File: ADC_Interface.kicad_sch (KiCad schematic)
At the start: 42 parts, among them U401 ADAU1978, U402 TLV333, X401 12.288MHz

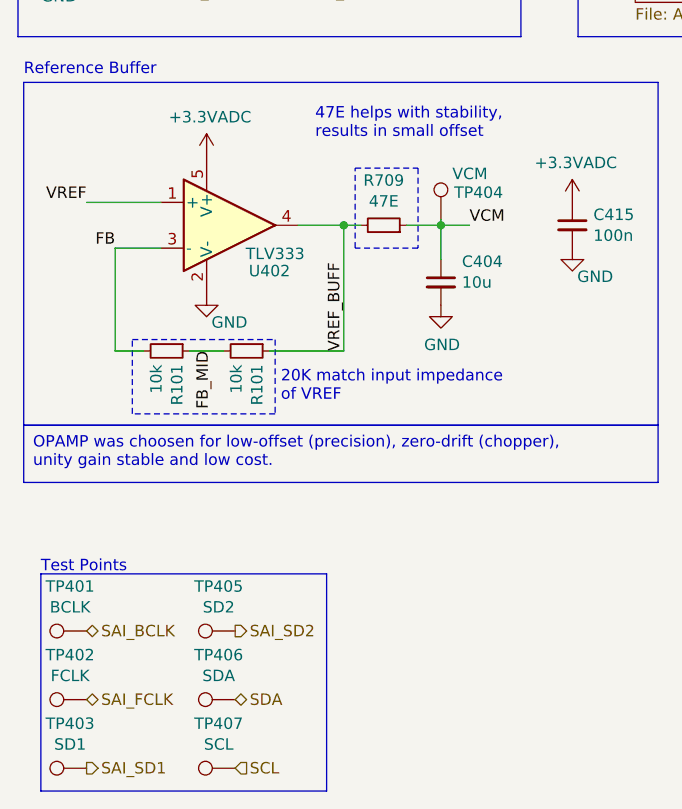
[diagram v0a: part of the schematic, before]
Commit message: (pcb) route power
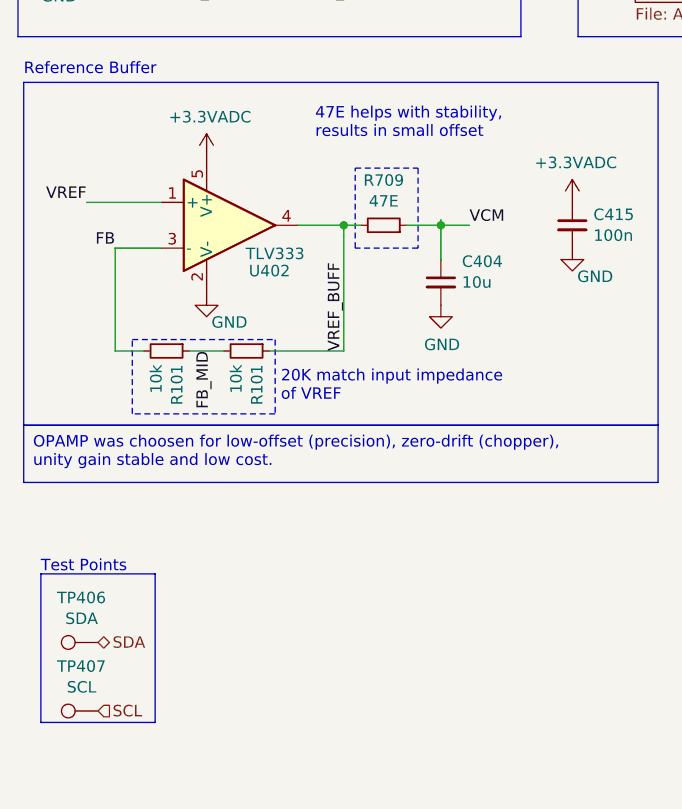
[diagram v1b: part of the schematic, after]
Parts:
- removed TP401: BCLK, TestPoint:TestPoint_Pad_D1.0mm, symbol Connector:TestPoint
- removed TP402: FCLK, TestPoint:TestPoint_Pad_D1.0mm, symbol Connector:TestPoint
- removed TP403: SD1, TestPoint:TestPoint_Pad_D1.0mm, symbol Connector:TestPoint
- removed TP404: VCM, TestPoint:TestPoint_Pad_D1.0mm, symbol Connector:TestPoint
- removed TP405: SD2, TestPoint:TestPoint_Pad_D1.0mm, symbol Connector:TestPoint
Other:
- moved on the sheet: TP406, TP407
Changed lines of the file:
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@@
     (fill (type none))
   )
-  (rectangle (start 20.32 152.4) (end 52.07 176.53)
+  (rectangle (start 20.32 152.4) (end 33.02 168.91)
     (stroke (width 0) (type default))
     (fill (type none))
@@
     (effects (font (size 1.27 1.27)) (justify left))
   )
-  (hierarchical_label "SDA" (shape bidirectional) (at 41.91 166.37 0) (fields_autoplaced)
-    (effects (font (size 1.27 1.27)) (justify left))
-  )
-  (hierarchical_label "SAI_BCLK" (shape bidirectional) (at 25.4 158.75 0) (fields_autoplaced)
-    (effects (font (size 1.27 1.27)) (justify left))
-  )
-  (hierarchical_label "SAI_SD2" (shape output) (at 41.91 158.75 0) (fields_autoplaced)
-    (effects (font (size 1.27 1.27)) (justify left))
-  )
-  (hierarchical_label "SAI_SD1" (shape output) (at 25.4 173.99 0) (fields_autoplaced)
+  (hierarchical_label "SDA" (shape bidirectional) (at 26.67 160.02 0) (fields_autoplaced)
     (effects (font (size 1.27 1.27)) (justify left))
   )
@@
     (effects (font (size 1.27 1.27)) (justify left))
   )
-  (hierarchical_label "SCL" (shape input) (at 41.91 173.99 0) (fields_autoplaced)
+  (hierarchical_label "SCL" (shape input) (at 26.67 167.64 0) (fields_autoplaced)
     (effects (font (size 1.27 1.27)) (justify left))
   )
   (hierarchical_label "SCL" (shape input) (at 260.35 104.14 0) (fields_autoplaced)
-    (effects (font (size 1.27 1.27)) (justify left))
-  )
-  (hierarchical_label "SAI_FCLK" (shape bidirectional) (at 25.4 166.37 0) (fields_autoplaced)
     (effects (font (size 1.27 1.27)) (justify left))
   )
@@
     )
   )
-  (symbol (lib_id "Connector:TestPoint") (at 64.77 113.03 0) (unit 1)
-    (in_bom yes) (on_board yes) (dnp no)
-    (property "Reference" "TP404" (at 66.2432 110.0328 0)
-      (effects (font (size 1.27 1.27)) (justify left))
-    )
-    (property "Value" "VCM" (at 66.04 107.95 0)
-      (effects (font (size 1.27 1.27)) (justify left))
-    )
-    (property "Footprint" "TestPoint:TestPoint_Pad_D1.0mm" (at 69.85 113.03 0)
-      (effects (font (size 1.27 1.27)) hide)
-    )
-    (property "Datasheet" "~" (at 69.85 113.03 0)
-      (effects (font (size 1.27 1.27)) hide)
-    )
-    (pin "1")
-    (instances
-      (project "kleinvoet"
-        (path "/4185c36c-c66e-4dbd-be5d-841e551f4885/00000000-0000-0000-0000-00005ee5ecad"
-          (reference "TP404") (unit 1)
-        )
-      )
-    )
-  )
-  (symbol (lib_id "Connector:TestPoint") (at 25.4 158.75 90) (unit 1)
-    (in_bom yes) (on_board yes) (dnp no)
-    (property "Reference" "TP401" (at 23.5712 153.797 90)
-      (effects (font (size 1.27 1.27)))
-    )
-    (property "Value" "BCLK" (at 23.5712 156.1084 90)
-      (effects (font (size 1.27 1.27)))
-    )
-    (property "Footprint" "TestPoint:TestPoint_Pad_D1.0mm" (at 25.4 153.67 0)
-      (effects (font (size 1.27 1.27)) hide)
-    )
-    (property "Datasheet" "~" (at 25.4 153.67 0)
-      (effects (font (size 1.27 1.27)) hide)
-    )
-    (pin "1")
-    (instances
-      (project "kleinvoet"
-        (path "/4185c36c-c66e-4dbd-be5d-841e551f4885/00000000-0000-0000-0000-00005ee5ecad"
-          (reference "TP401") (unit 1)
-        )
-      )
-    )
-  )
-  (symbol (lib_id "Connector:TestPoint") (at 25.4 166.37 90) (unit 1)
-    (in_bom yes) (on_board yes) (dnp no)
-    (property "Reference" "TP402" (at 23.5712 161.417 90)
-      (effects (font (size 1.27 1.27)))
-    )
-    (property "Value" "FCLK" (at 23.5712 163.7284 90)
-      (effects (font (size 1.27 1.27)))
-    )
-    (property "Footprint" "TestPoint:TestPoint_Pad_D1.0mm" (at 25.4 161.29 0)
-      (effects (font (size 1.27 1.27)) hide)
-    )
-    (property "Datasheet" "~" (at 25.4 161.29 0)
-      (effects (font (size 1.27 1.27)) hide)
-    )
-    (pin "1")
-    (instances
-      (project "kleinvoet"
-        (path "/4185c36c-c66e-4dbd-be5d-841e551f4885/00000000-0000-0000-0000-00005ee5ecad"
-          (reference "TP402") (unit 1)
-        )
-      )
-    )
-  )
-  (symbol (lib_id "Connector:TestPoint") (at 25.4 173.99 90) (unit 1)
-    (in_bom yes) (on_board yes) (dnp no)
-    (property "Reference" "TP403" (at 23.5712 169.037 90)
-      (effects (font (size 1.27 1.27)))
-    )
-    (property "Value" "SD1" (at 23.5712 171.3484 90)
-      (effects (font (size 1.27 1.27)))
-    )
-    (property "Footprint" "TestPoint:TestPoint_Pad_D1.0mm" (at 25.4 168.91 0)
-      (effects (font (size 1.27 1.27)) hide)
-    )
-    (property "Datasheet" "~" (at 25.4 168.91 0)
-      (effects (font (size 1.27 1.27)) hide)
-    )
-    (pin "1")
-    (instances
-      (project "kleinvoet"
-        (path "/4185c36c-c66e-4dbd-be5d-841e551f4885/00000000-0000-0000-0000-00005ee5ecad"
-          (reference "TP403") (unit 1)
-        )
-      )
-    )
-  )
-  (symbol (lib_id "Connector:TestPoint") (at 41.91 158.75 90) (unit 1)
-    (in_bom yes) (on_board yes) (dnp no)
-    (property "Reference" "TP405" (at 40.0812 153.797 90)
-      (effects (font (size 1.27 1.27)))
-    )
-    (property "Value" "SD2" (at 40.0812 156.1084 90)
-      (effects (font (size 1.27 1.27)))
-    )
-    (property "Footprint" "TestPoint:TestPoint_Pad_D1.0mm" (at 41.91 153.67 0)
-      (effects (font (size 1.27 1.27)) hide)
-    )
-    (property "Datasheet" "~" (at 41.91 153.67 0)
-      (effects (font (size 1.27 1.27)) hide)
-    )
-    (pin "1")
-    (instances
-      (project "kleinvoet"
-        (path "/4185c36c-c66e-4dbd-be5d-841e551f4885/00000000-0000-0000-0000-00005ee5ecad"
-          (reference "TP405") (unit 1)
-        )
-      )
-    )
-  )
-  (symbol (lib_id "Connector:TestPoint") (at 41.91 166.37 90) (unit 1)
-    (in_bom yes) (on_board yes) (dnp no)
-    (property "Reference" "TP406" (at 40.0812 161.417 90)
-      (effects (font (size 1.27 1.27)))
-    )
-    (property "Value" "SDA" (at 40.0812 163.7284 90)
-      (effects (font (size 1.27 1.27)))
-    )
-    (property "Footprint" "TestPoint:TestPoint_Pad_D1.0mm" (at 41.91 161.29 0)
-      (effects (font (size 1.27 1.27)) hide)
-    )
-    (property "Datasheet" "~" (at 41.91 161.29 0)
+  (symbol (lib_id "Connector:TestPoint") (at 26.67 160.02 90) (unit 1)
+    (in_bom yes) (on_board yes) (dnp no)
+    (property "Reference" "TP406" (at 24.8412 155.067 90)
+      (effects (font (size 1.27 1.27)))
+    )
+    (property "Value" "SDA" (at 24.8412 157.3784 90)
+      (effects (font (size 1.27 1.27)))
+    )
+    (property "Footprint" "TestPoint:TestPoint_Pad_D1.0mm" (at 26.67 154.94 0)
+      (effects (font (size 1.27 1.27)) hide)
+    )
+    (property "Datasheet" "~" (at 26.67 154.94 0)
       (effects (font (size 1.27 1.27)) hide)
     )
@@
     )
   )
-  (symbol (lib_id "Connector:TestPoint") (at 41.91 173.99 90) (unit 1)
-    (in_bom yes) (on_board yes) (dnp no)
-    (property "Reference" "TP407" (at 40.0812 169.037 90)
-      (effects (font (size 1.27 1.27)))
-    )
-    (property "Value" "SCL" (at 40.0812 171.3484 90)
-      (effects (font (size 1.27 1.27)))
-    )
-    (property "Footprint" "TestPoint:TestPoint_Pad_D1.0mm" (at 41.91 168.91 0)
-      (effects (font (size 1.27 1.27)) hide)
-    )
-    (property "Datasheet" "~" (at 41.91 168.91 0)
-      (effects (font (size 1.27 1.27)) hide)
-    )
+  (symbol (lib_id "Connector:TestPoint") (at 26.67 167.64 90) (unit 1)
+    (in_bom yes) (on_board yes) (dnp no)
+    (property "Reference" "TP407" (at 24.8412 162.687 90)
+      (effects (font (size 1.27 1.27)))
+    )
+    (property "Value" "SCL" (at 24.8412 164.9984 90)
+      (effects (font (size 1.27 1.27)))
+    )
+    (property "Footprint" "TestPoint:TestPoint_Pad_D1.0mm" (at 26.67 162.56 0)
+      (effects (font (size 1.27 1.27)) hide)
+    )
+    (property "Datasheet" "~" (at 26.67 162.56 0)
+      (effects (font (size 1.27 1.27)) hide)
+    )

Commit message: (pcb) route VCC to audio conn.
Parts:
- added C416, C417: 10u, Capacitor_SMD:C_0402_1005Metric, symbol Device:C_Small
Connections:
- net +3.3VADC: now also CB401.1, R904.1, R904.2, X401.4 (VDD)
- net +3V3: no longer CB401.1, R904.1, R904.2, X401.4 (VDD)
- net GND: now also C416.2, C417.2
- net VCC: now also C416.1, C417.1
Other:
- moved on the sheet: C404, C415, R101, R709, TP406, TP407, U402

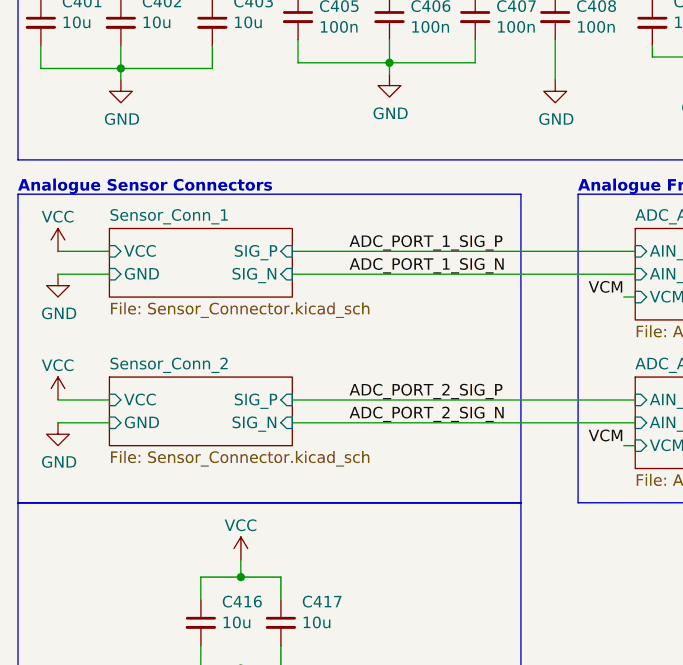
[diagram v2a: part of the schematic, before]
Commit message: (sch) add analogue VCC load switch
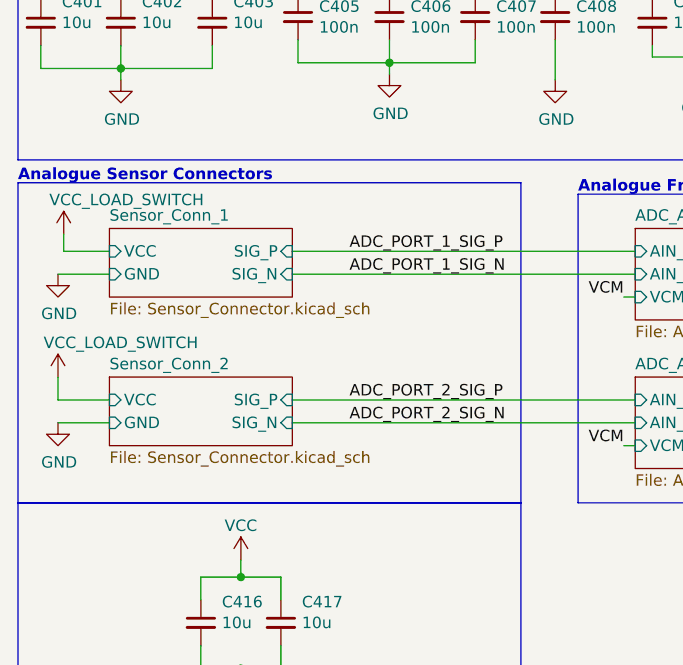
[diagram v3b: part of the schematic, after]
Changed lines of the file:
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@@
+    (stroke (width 0) (type default))
+  )
+  (wire (pts (xy 22.225 78.74) (xy 22.225 81.28))
     (stroke (width 0) (type default))
   )
@@
     (stroke (width 0) (type default))
   )
-  (polyline (pts (xy 73.66 58.42) (xy 73.66 92.71))
+  (polyline (pts (xy 73.66 57.15) (xy 73.66 92.71))
     (stroke (width 0) (type default))
   )
@@
     (stroke (width 0) (type default))
   )
+  (wire (pts (xy 22.86 62.865) (xy 22.86 64.77))
+    (stroke (width 0) (type default))
+  )
   (wire (pts (xy 129.54 36.195) (xy 129.54 33.655))
     (stroke (width 0) (type default))
@@
     (stroke (width 0) (type default))
   )
+  (wire (pts (xy 22.86 64.77) (xy 27.94 64.77))
+    (stroke (width 0) (type default))
+  )
   (wire (pts (xy 170.815 140.97) (xy 170.815 139.7))
     (stroke (width 0) (type default))
@@
     (stroke (width 0) (type default))
   )
-  (wire (pts (xy 22.225 64.77) (xy 27.94 64.77))
-    (stroke (width 0) (type default))
-  )
   (wire (pts (xy 20.32 44.45) (xy 20.32 41.91))
     (stroke (width 0) (type default))
@@
     (stroke (width 0) (type default))
   )
-  (polyline (pts (xy 17.78 58.42) (xy 73.66 58.42))
+  (polyline (pts (xy 17.78 57.15) (xy 73.66 57.15))
     (stroke (width 0) (type default))
   )
@@
     (stroke (width 0) (type default))
   )
-  (polyline (pts (xy 17.78 58.42) (xy 17.78 92.71))
+  (polyline (pts (xy 17.78 57.15) (xy 17.78 92.71))
     (stroke (width 0) (type default))
   )
@@
     (effects (font (size 1.27 1.27)) (justify left bottom))
   )
-  (text "Analogue Sensor Connectors" (at 17.78 58.42 0)
+  (text "Analogue Sensor Connectors" (at 17.78 57.15 0)
     (effects (font (size 1.27 1.27) (thickness 0.254) bold) (justify left bottom))
   )
@@
     )
   )
-  (symbol (lib_id "power:VCC") (at 22.225 81.28 0) (unit 1)
-    (in_bom yes) (on_board yes) (dnp no) (fields_autoplaced)
-    (property "Reference" "#PWR08" (at 22.225 85.09 0)
-      (effects (font (size 1.27 1.27)) hide)
-    )
-    (property "Value" "VCC" (at 22.225 77.47 0)
-      (effects (font (size 1.27 1.27)))
-    )
-    (property "Footprint" "" (at 22.225 81.28 0)
-      (effects (font (size 1.27 1.27)) hide)
-    )
-    (property "Datasheet" "" (at 22.225 81.28 0)
-      (effects (font (size 1.27 1.27)) hide)
-    )
-    (pin "1")
-    (instances
-      (project "kleinvoet"
-        (path "/4185c36c-c66e-4dbd-be5d-841e551f4885/00000000-0000-0000-0000-00005ee5ecad"
-          (reference "#PWR08") (unit 1)
-        )
-      )
-    )
-  )
   (symbol (lib_id "power:GND") (at 29.21 45.72 0) (unit 1)
     (in_bom yes) (on_board yes) (dnp no)
@@
         (path "/4185c36c-c66e-4dbd-be5d-841e551f4885/00000000-0000-0000-0000-00005ee5ecad"
           (reference "R411") (unit 1)
+        )
+      )
+    )
+  )
+  (symbol (lib_id "grootvoet:VCC_LOAD_SWITCH") (at 22.225 78.74 0) (unit 1)
+    (in_bom yes) (on_board yes) (dnp no)
+    (property "Reference" "#PWR0952" (at 22.225 82.55 0)
+      (effects (font (size 1.27 1.27)) hide)
+    )
+    (property "Value" "VCC_LOAD_SWITCH" (at 29.21 74.93 0)
+      (effects (font (size 1.27 1.27)))
+    )
+    (property "Footprint" "" (at 22.225 78.74 0)
+      (effects (font (size 1.27 1.27)) hide)
+    )
+    (property "Datasheet" "" (at 22.225 78.74 0)
+      (effects (font (size 1.27 1.27)) hide)
+    )
+    (pin "1")
+    (instances
+      (project "kleinvoet"
+        (path "/4185c36c-c66e-4dbd-be5d-841e551f4885/00000000-0000-0000-0000-00005eede770"
+          (reference "#PWR0952") (unit 1)
+        )
+        (path "/4185c36c-c66e-4dbd-be5d-841e551f4885/00000000-0000-0000-0000-00005ee5ecad"
+          (reference "#PWR0431") (unit 1)
         )
       )
@@
     )
   )
-  (symbol (lib_id "power:VCC") (at 22.225 64.77 0) (unit 1)
-    (in_bom yes) (on_board yes) (dnp no) (fields_autoplaced)
-    (property "Reference" "#PWR09" (at 22.225 68.58 0)
-      (effects (font (size 1.27 1.27)) hide)
-    )
-    (property "Value" "VCC" (at 22.225 60.96 0)
-      (effects (font (size 1.27 1.27)))
-    )
-    (property "Footprint" "" (at 22.225 64.77 0)
-      (effects (font (size 1.27 1.27)) hide)
-    )
-    (property "Datasheet" "" (at 22.225 64.77 0)
-      (effects (font (size 1.27 1.27)) hide)
-    )
-    (pin "1")
-    (instances
-      (project "kleinvoet"
-        (path "/4185c36c-c66e-4dbd-be5d-841e551f4885/00000000-0000-0000-0000-00005ee5ecad"
-          (reference "#PWR09") (unit 1)
-        )
-      )
-    )
-  )
   (symbol (lib_id "Device:R_Small") (at 129.54 38.735 0) (unit 1)
     (in_bom yes) (on_board yes) (dnp no)
@@
         )
       )
+    )
+  )
+  (symbol (lib_id "grootvoet:VCC_LOAD_SWITCH") (at 22.86 62.865 0) (unit 1)
+    (in_bom yes) (on_board yes) (dnp no)
+    (property "Reference" "#PWR0952" (at 22.86 66.675 0)
+      (effects (font (size 1.27 1.27)) hide)
+    )
+    (property "Value" "VCC_LOAD_SWITCH" (at 29.845 59.055 0)
+      (effects (font (size 1.27 1.27)))
+    )
+    (property "Footprint" "" (at 22.86 62.865 0)
+      (effects (font (size 1.27 1.27)) hide)
+    )
+    (property "Datasheet" "" (at 22.86 62.865 0)
+      (effects (font (size 1.27 1.27)) hide)
+    )
+    (pin "1")
+    (instances
+      (project "kleinvoet"
+        (path "/4185c36c-c66e-4dbd-be5d-841e551f4885/00000000-0000-0000-0000-00005eede770"
+          (reference "#PWR0952") (unit 1)
+        )
+        (path "/4185c36c-c66e-4dbd-be5d-841e551f4885/00000000-0000-0000-0000-00005ee5ecad"
+          (reference "#PWR0435") (unit 1)
+        )
+      )

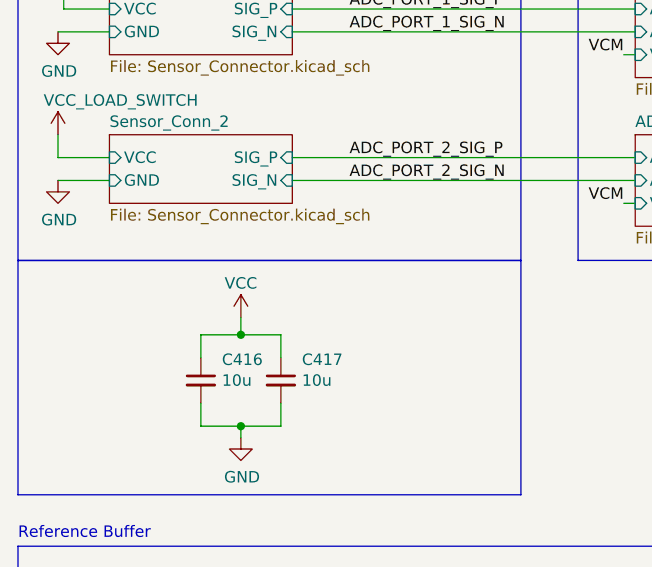
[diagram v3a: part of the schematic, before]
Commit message: (pcb) initial load switch layout
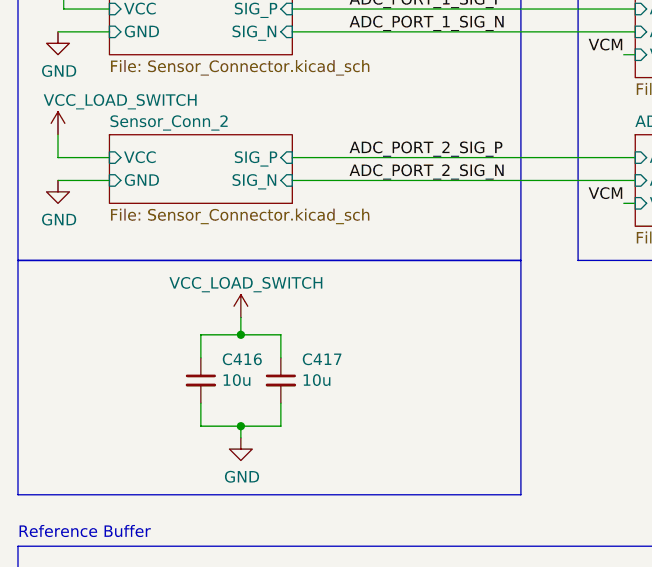
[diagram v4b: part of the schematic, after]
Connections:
- net VCC is gone; now on net VCC_LOAD_SWITCH: C416.1, C417.1
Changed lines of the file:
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@@
-    )
-  )
-  (symbol (lib_id "power:VCC") (at 42.545 99.06 0) (unit 1)
-    (in_bom yes) (on_board yes) (dnp no) (fields_autoplaced)
-    (property "Reference" "#PWR0426" (at 42.545 102.87 0)
-      (effects (font (size 1.27 1.27)) hide)
-    )
-    (property "Value" "VCC" (at 42.545 95.25 0)
-      (effects (font (size 1.27 1.27)))
-    )
-    (property "Footprint" "" (at 42.545 99.06 0)
-      (effects (font (size 1.27 1.27)) hide)
-    )
-    (property "Datasheet" "" (at 42.545 99.06 0)
-      (effects (font (size 1.27 1.27)) hide)
-    )
-    (pin "1")
-    (instances
-      (project "kleinvoet"
-        (path "/4185c36c-c66e-4dbd-be5d-841e551f4885/00000000-0000-0000-0000-00005ee5ecad"
-          (reference "#PWR0426") (unit 1)
-        )
-      )
     )
   )
@@
         )
       )
+    )
+  )
+  (symbol (lib_id "grootvoet:VCC_LOAD_SWITCH") (at 42.545 99.06 0) (unit 1)
+    (in_bom yes) (on_board yes) (dnp no)
+    (property "Reference" "#PWR0952" (at 42.545 102.87 0)
+      (effects (font (size 1.27 1.27)) hide)
+    )
+    (property "Value" "VCC_LOAD_SWITCH" (at 43.18 95.25 0)
+      (effects (font (size 1.27 1.27)))
+    )
+    (property "Footprint" "" (at 42.545 99.06 0)
+      (effects (font (size 1.27 1.27)) hide)
+    )
+    (property "Datasheet" "" (at 42.545 99.06 0)
+      (effects (font (size 1.27 1.27)) hide)
+    )
+    (pin "1")
+    (instances
+      (project "kleinvoet"
+        (path "/4185c36c-c66e-4dbd-be5d-841e551f4885/00000000-0000-0000-0000-00005eede770"
+          (reference "#PWR0952") (unit 1)
+        )
+        (path "/4185c36c-c66e-4dbd-be5d-841e551f4885/00000000-0000-0000-0000-00005ee5ecad"
+          (reference "#PWR0426") (unit 1)
+        )
+      )

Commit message: (sch) run DRC
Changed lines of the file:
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@@
     (effects (font (size 1.27 1.27) (thickness 0.254) bold) (justify left bottom))
-  )
-  (label "SA_MODE" (at 210.185 130.81 0) (fields_autoplaced)
-    (effects (font (size 1.27 1.27)) (justify left bottom))
   )
   (label "ADC_2_P" (at 142.875 119.38 180) (fields_autoplaced)
@@
     (effects (font (size 1.27 1.27) italic) (justify left bottom))
   )
-  (label "LRCLK" (at 210.185 88.9 0) (fields_autoplaced)
-    (effects (font (size 1.27 1.27)) (justify left bottom))
-  )
   (hierarchical_label "SAI_BCLK" (shape bidirectional) (at 236.22 86.36 0) (fields_autoplaced)

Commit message: (sch) consoldate BOM
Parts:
- U402: MPN (none) -> TLV333IDCKR; Mfr. (none) -> Texas Instruments
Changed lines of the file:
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@@
       (effects (font (size 1.27 1.27)) hide)
     )
-    (property "MPN" "" (at 40.64 140.335 0)
+    (property "MPN" "TLV333IDCKR" (at 40.64 140.335 0)
       (effects (font (size 1.27 1.27)) hide)
     )
-    (property "Mfr." "" (at 40.64 140.335 0)
+    (property "Mfr." "Texas Instruments" (at 40.64 140.335 0)
       (effects (font (size 1.27 1.27)) hide)
     )
